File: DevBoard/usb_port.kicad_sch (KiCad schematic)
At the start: 101 parts, among them J501 TYPE-C 16PCB0.8 IP68, J502 I2CC logic analyzer, Q501 IAUC45N04S6L063H, Q502 IAUC45N04S6L063H, U501 TPS25751DREFR, U502 M24512-DFMC6TG, U503 BQ25756RRVR, U504 TPS62933DRLR

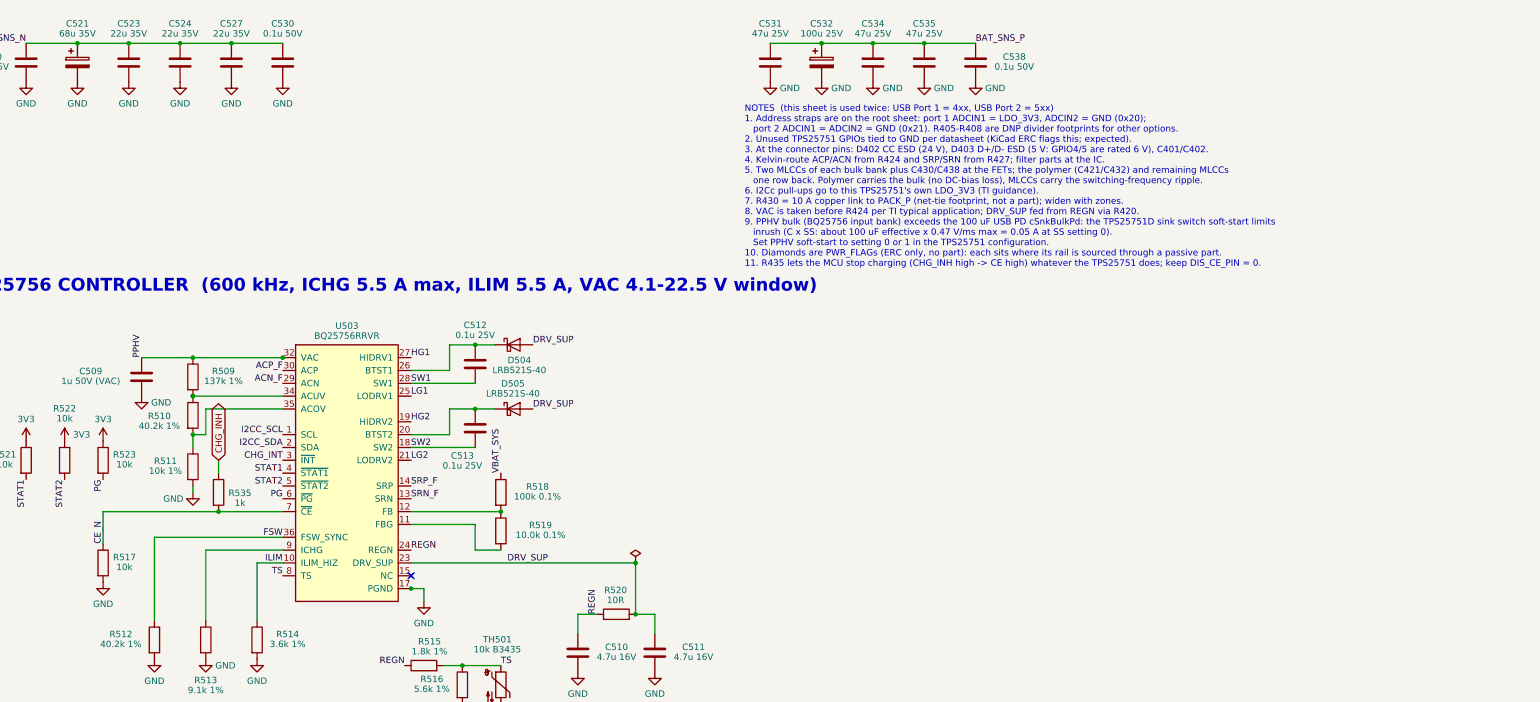
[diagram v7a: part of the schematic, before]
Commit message: Dev board rev A5: FET ESD caps, review 2, fail-safe CHG_INH, MCU I/O plan
- Gauge: C110/C111 (2 x 0.1 uF in series) across the protection FET pair,
  TI BQ40Z50-R2 fig. 9-2 C1/C2; C107/C108 across PACK+/PACK- unchanged.
- Second 3-reviewer schematic review with a challenge round
  (docs/devboard/schematic-review-2-2026-10-12.md, raw files in review2/):
  0 critical, 1 major (gauge precharge config), hardware proposals listed.
- CHG_INH now fails safe: R417/R517 47k pull-up on CE to 3V3; the MCU
  drives PB8 low to allow charging. MCU IWDG in hardware mode.
- Decisions: ICHG stays 9.1k; F101 stays 15 A with a gauge cut-off of
  2.8 V/cell or higher under load.
- docs/devboard/mcu-io-power-states.md: every MCU pin per power state,
  reconciled with the 150 uA sleep budget (PB8 low only while charging).

Co-Authored-By: Claude Opus 5.5 <noreply@anthropic.com>
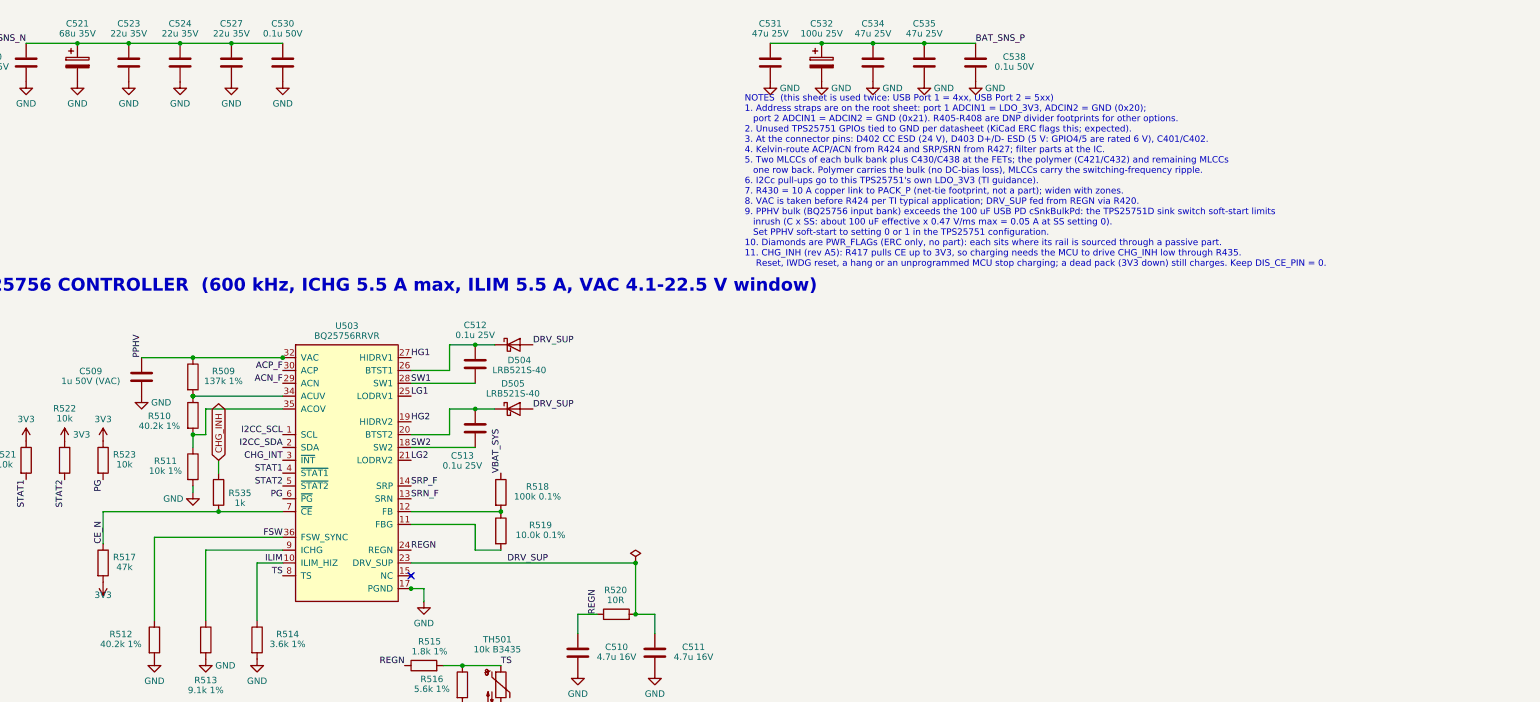
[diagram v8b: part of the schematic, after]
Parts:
- R517: value 10k -> 47k; LCSC (none) -> C25819; MPN (none) -> 0603WAF4702T5E; Notes CE low = charge on -> CE pull-up to 3V3: charging is inhibited unless the MCU dri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
- R535: Notes CHG_INH from the MCU (PB8): high stops charging at the CE p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 -> CHG_INH from the MCU (PB8): low allows charging; high or hi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
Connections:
- net 3V3: now also R517.2
- net GND: no longer R517.2
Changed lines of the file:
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@@
 		)
 	)
-	(text "NOTES  (this sheet is used twice: USB Port 1 = 4xx, USB Port 2 = 5xx)\n1. Address straps are on the root sheet: port 1 ADCIN1 = LDO_3V3, ADCIN2 = GND (0x20);\n   port 2 ADCIN1 = ADCIN2 = GND (0x21). R405-R408 are DNP divider footprints for other options.\n2. Unused TPS25751 GPIOs tied to GND per datasheet (KiCad ERC flags this; expected).\n3. At the connector pins: D402 CC ESD (24 V), D403 D+/D- ESD (5 V: GPIO4/5 are rated 6 V), C401/C402.\n4. Kelvin-route ACP/ACN from R424 and SRP/SRN from R427; filter parts at the IC.\n5. Two MLCCs of each bulk bank plus C430/C438 at the FETs; the polymer (C421/C432) and remaining MLCCs\n   one row back. Polymer carries the bulk (no DC-bias loss), MLCCs carry the switching-frequency ripple.\n6. I2Cc pull-ups go to this TPS25751's own LDO_3V3 (TI guidance).\n7. R430 = 10 A copper link to PACK_P (net-tie footprint, not a part); widen with zones.\n8. VAC is taken before R424 per TI typical application; DRV_SUP fed from REGN via R420.\n9. PPHV bulk (BQ25756 input bank) exceeds the 100 uF USB PD cSnkBulkPd: the TPS25751D sink switch soft-start limits\n   inrush (C x SS: about 100 uF effective x 0.47 V/ms max = 0.05 A at SS setting 0).\n   Set PPHV soft-start to setting 0 or 1 in the TPS25751 configuration.\n10. Diamonds are PWR_FLAGs (ERC only, no part): each sits where its rail is sourced through a passive part.\n11. R435 lets the MCU stop charging (CHG_INH high -> CE high) whatever the TPS25751 does; keep DIS_CE_PIN = 0."
+	(text "NOTES  (this sheet is used twice: USB Port 1 = 4xx, USB Port 2 = 5xx)\n1. Address straps are on the root sheet: port 1 ADCIN1 = LDO_3V3, ADCIN2 = GND (0x20);\n   port 2 ADCIN1 = ADCIN2 = GND (0x21). R405-R408 are DNP divider footprints for other options.\n2. Unused TPS25751 GPIOs tied to GND per datasheet (KiCad ERC flags this; expected).\n3. At the connector pins: D402 CC ESD (24 V), D403 D+/D- ESD (5 V: GPIO4/5 are rated 6 V), C401/C402.\n4. Kelvin-route ACP/ACN from R424 and SRP/SRN from R427; filter parts at the IC.\n5. Two MLCCs of each bulk bank plus C430/C438 at the FETs; the polymer (C421/C432) and remaining MLCCs\n   one row back. Polymer carries the bulk (no DC-bias loss), MLCCs carry the switching-frequency ripple.\n6. I2Cc pull-ups go to this TPS25751's own LDO_3V3 (TI guidance).\n7. R430 = 10 A copper link to PACK_P (net-tie footprint, not a part); widen with zones.\n8. VAC is taken before R424 per TI typical application; DRV_SUP fed from REGN via R420.\n9. PPHV bulk (BQ25756 input bank) exceeds the 100 uF USB PD cSnkBulkPd: the TPS25751D sink switch soft-start limits\n   inrush (C x SS: about 100 uF effective x 0.47 V/ms max = 0.05 A at SS setting 0).\n   Set PPHV soft-start to setting 0 or 1 in the TPS25751 configuration.\n10. Diamonds are PWR_FLAGs (ERC only, no part): each sits where its rail is sourced through a passive part.\n11. CHG_INH (rev A5): R417 pulls CE up to 3V3, so charging needs the MCU to drive CHG_INH low through R435.\n    Reset, IWDG reset, a hang or an unprogrammed MCU stop charging; a dead pack (3V3 down) still charges. Keep DIS_CE_PIN = 0."
 		(exclude_from_sim no)
 		(at 459.74 162.56 0)
@@
 	)
 	(symbol
-		(lib_id "power:GND")
-		(at 332.74 224.79 0)
-		(unit 1)
-		(body_style 1)
-		(exclude_from_sim no)
-		(in_bom yes)
-		(on_board yes)
-		(in_pos_files yes)
-		(dnp no)
-		(property "Reference" "#PWR555"
-			(at 332.74 224.79 0)
-			(hide yes)
-			(show_name no)
-			(do_not_autoplace no)
-			(effects
-				(font
-					(size 1.27 1.27)
-				)
-			)
-		)
-		(property "Value" "GND"
-			(at 332.74 229.11 0)
-			(show_name no)
-			(do_not_autoplace no)
-			(effects
-				(font
-					(size 1.27 1.27)
-				)
-			)
-		)
-		(property "Footprint" ""
-			(at 332.74 224.79 0)
-			(hide yes)
-			(show_name no)
-			(do_not_autoplace no)
-			(effects
-				(font
-					(size 1.27 1.27)
-				)
-			)
-		)
-		(property "Datasheet" ""
-			(at 332.74 224.79 0)
-			(hide yes)
-			(show_name no)
-			(do_not_autoplace no)
-			(effects
-				(font
-					(size 1.27 1.27)
-				)
-			)
-		)
-		(property "Description" "Power symbol creates a global label with name \"GND\" , ground"
-			(at 332.74 224.79 0)
-			(hide yes)
-			(show_name no)
-			(do_not_autoplace no)
-			(effects
-				(font
-					(size 1.27 1.27)
-				)
-			)
-		)
-		(pin "1"
-		)
-		(instances
-			(project "MonolithDev"
-				(path "/f83241ae-2bb3-4ed7-b986-c0a03971de0a/5279a7a1-113d-4a80-b1cf-737ba19b6809"
-					(reference "#PWR555")
-					(unit 1)
-				)
-				(path "/f83241ae-2bb3-4ed7-b986-c0a03971de0a/ac72c9a4-7723-4f18-89ba-289142807a08"
-					(reference "#PWR455")
-					(unit 1)
-				)
-			)
-		)
-	)
-	(symbol
 		(lib_id "Device:R")
 		(at 218.44 144.78 0)
@@
 			)
 		)
-		(property "Value" "10k"
+		(property "Value" "47k"
 			(at 336.97 221.81 0)
 			(show_name no)
@@
 			)
 		)
-		(property "Notes" "CE low = charge on"
+		(property "Notes" "CE pull-up to 3V3: charging is inhibited unless the MCU drives CHG_INH low (reset, hang, unprogrammed or Standby all inhibit). With 3V3 down (dead pack) CE reads low, so USB can still revive the pack. MCU low through R435: CE = 3.3 x 1k/48k = 0.07 V (VIL max 0.4 V)"
 			(at 0 0 0)
 			(hide yes)
@@
 			)
 		)
+		(property "LCSC" "C25819"
+			(at 332.74 220.98 0)
+			(hide yes)
+			(show_name no)
+			(do_not_autoplace no)
+			(effects
+				(font
+					(size 1.27 1.27)
+				)
+			)
+		)
+		(property "MPN" "0603WAF4702T5E"
+			(at 332.74 220.98 0)
+			(hide yes)
+			(show_name no)
+			(do_not_autoplace no)
+			(effects
+				(font
+					(size 1.27 1.27)
+				)
+			)
+		)
 		(pin "1"
 		)
@@
 			)
 		)
-		(property "Notes" "CHG_INH from the MCU (PB8): high stops charging at the CE pin, independent of the TPS25751. Off/reset MCU leaves CE pulled low by R417 (charging allowed). Keep DIS_CE_PIN = 0"
+		(property "Notes" "CHG_INH from the MCU (PB8): low allows charging; high or hi-Z (reset, IWDG reset, unprogrammed) stops it at the CE pin via the R417 pull-up, independent of the TPS25751. Keep DIS_CE_PIN = 0"
 			(at 355.6 207.01 0)
 			(hide yes)
@@
 		(color 0 0 0 0)
 	)
+	(symbol
+		(lib_id "power:+3V3")
+		(at 332.74 224.79 180)
+		(unit 1)
+		(body_style 1)
+		(exclude_from_sim no)
+		(in_bom no)
+		(on_board no)
+		(in_pos_files no)
+		(dnp no)
+		(property "Reference" "#PWR537"
+			(at 332.74 222.25 0)
+			(hide yes)
+			(show_name no)
+			(do_not_autoplace no)
+			(effects
+				(font
+					(size 1.27 1.27)
+				)
+			)
+		)
+		(property "Value" "3V3"
+			(at 332.74 227.32999999999998 0)
+			(show_name no)
+			(do_not_autoplace no)
+			(effects
+				(font
+					(size 1.27 1.27)
+				)
+			)
+		)
+		(property "Footprint" ""
+			(at 332.74 224.79 0)
+			(hide yes)
+			(show_name no)
+			(do_not_autoplace no)
+			(effects
+				(font
+					(size 1.27 1.27)
+				)
+			)
+		)
+		(property "Datasheet" ""
+			(at 332.74 224.79 0)
+			(hide yes)
+			(show_name no)
+			(do_not_autoplace no)
+			(effects
+				(font
+					(size 1.27 1.27)
+				)
+			)
+		)
+		(property "Description" ""
+			(at 332.74 224.79 0)
+			(hide yes)
+			(show_name no)
+			(do_not_autoplace no)
+			(effects
+				(font
+					(size 1.27 1.27)
+				)
+			)
+		)
+		(pin "1"
+		)
+		(instances
+			(project "MonolithDev"
+				(path "/f83241ae-2bb3-4ed7-b986-c0a03971de0a/5279a7a1-113d-4a80-b1cf-737ba19b6809"
+					(reference "#PWR537")
+					(unit 1)
+				)
+				(path "/f83241ae-2bb3-4ed7-b986-c0a03971de0a/ac72c9a4-7723-4f18-89ba-289142807a08"
+					(reference "#PWR437")
+					(unit 1)
+				)
+			)
+		)
+	)
 	(sheet_instances
